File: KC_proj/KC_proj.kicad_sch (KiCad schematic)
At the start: 30 parts, among them J1 Conn_01x05_Socket, J3 USB_C_Receptacle_USB2.0_14P, SW1 SW_Push, SW2 SW_Push, U1 STM32C071KBTx, U2 AMS1117-3.3, U4 TPS2116DRL

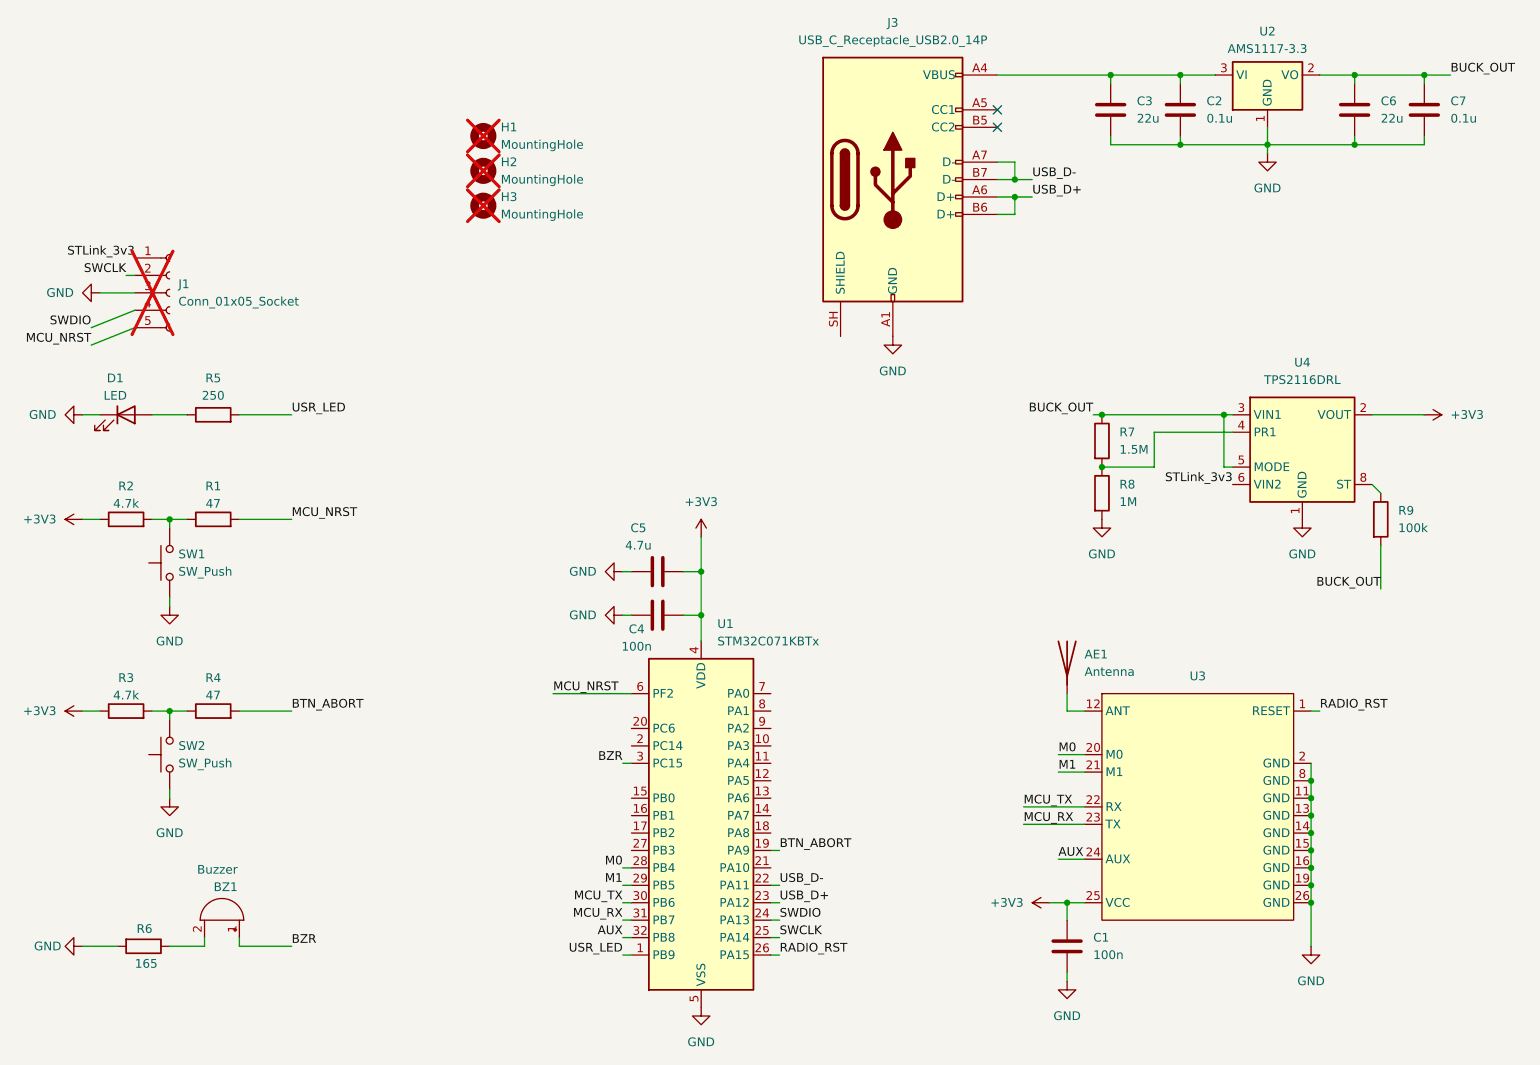
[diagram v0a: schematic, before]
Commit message: Update libs and kicad
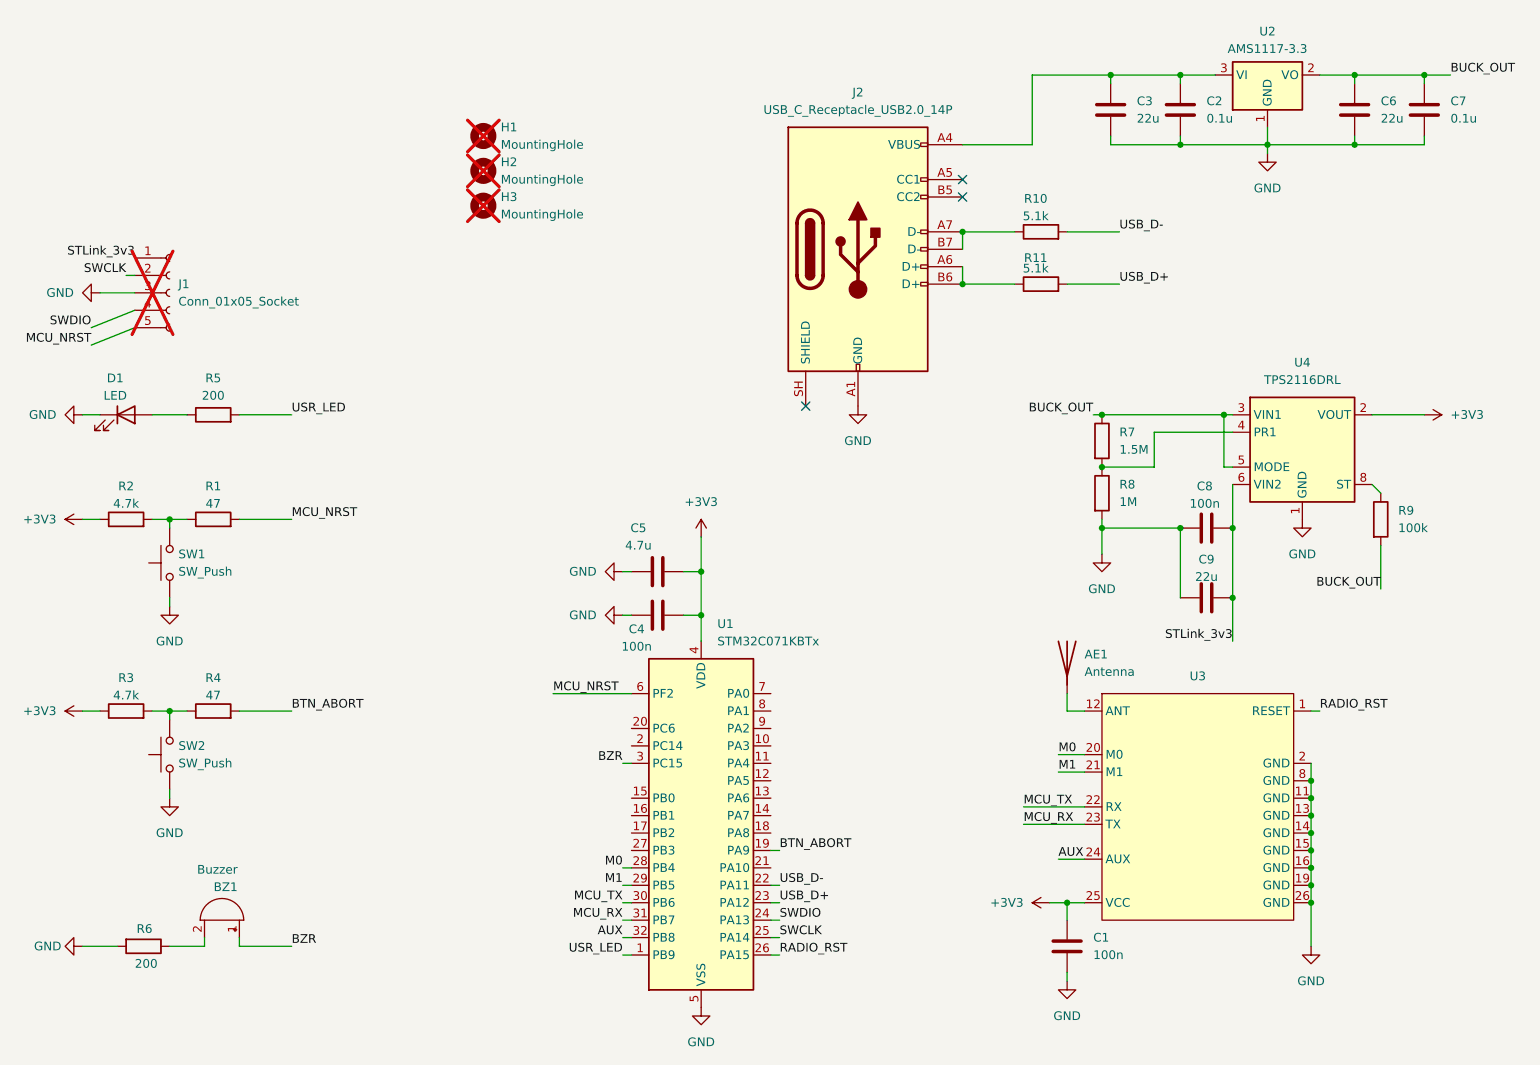
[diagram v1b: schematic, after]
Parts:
- removed J3: USB_C_Receptacle_USB2.0_14P, Connector_USB:USB_C_Receptacle_HRO_TYPE-C-31-M-12, symbol Connector:USB_C_Receptacle_USB2.0_14P
- added C8: 100n, Capacitor_SMD:C_0603_1608Metric, symbol Device:C
- added C9: 22u, Capacitor_SMD:C_0603_1608Metric, symbol Device:C
- added J2: USB_C_Receptacle_USB2.0_14P, Connector_USB:USB_C_Receptacle_HRO_TYPE-C-31-M-12, symbol Connector:USB_C_Receptacle_USB2.0_14P
- added R10, R11: 5.1k, Resistor_SMD:R_0603_1608Metric, symbol Device:R
- D1: footprint LED_SMD:LED_1206_3216Metric -> LED_SMD:LED_0603_1608Metric
- R5: value 250 -> 200
- R6: value 165 -> 200
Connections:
- net GND: now also C8.1, C9.1, J2.A1 (GND), J2.A12 (GND), J2.B1 (GND), J2.B12 (GND)
- net STLink_3v3: now also C8.2, C9.2
- net USB_D+: now also R11.2
- net USB_D-: now also R10.2
- net at C2.1, C3.1, U2.3 (VI): now also J2.A4 (VBUS), J2.A9 (VBUS), J2.B4 (VBUS), J2.B9 (VBUS)
- new net: J2.A7 (D-), J2.B7 (D-), R10.1
- new net: J2.A6 (D+), J2.B6 (D+), R11.1
- no-connect marks 2 -> 3
